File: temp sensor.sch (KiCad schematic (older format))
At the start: 28 parts, among them IC1 ESP32-C3-MINI-1, J1 Conn_01x02_Male, J2 Conn_01x04_Male, J3 Conn_01x05_Male, J4 USB_B_Micro, U2 TLV62569DBV, U3 BME280, U4 Si7020-A20, U5 SN65220

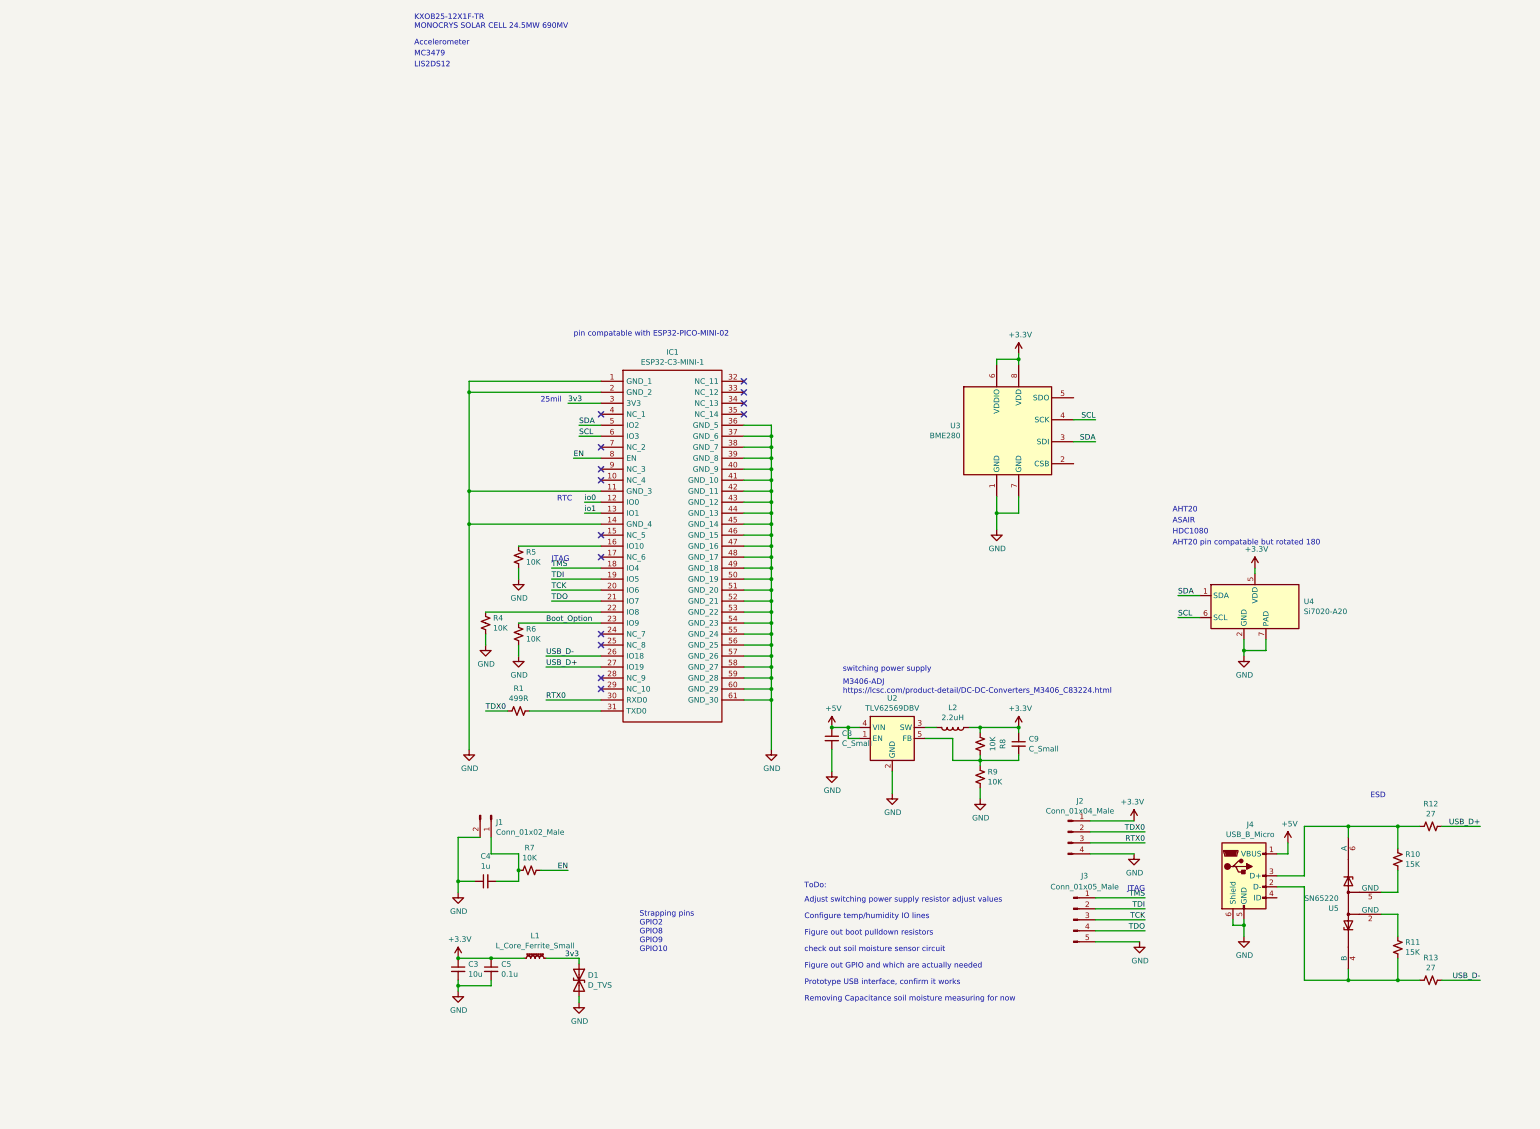
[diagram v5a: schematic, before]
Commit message: layout and part changes
Signed-off-by: lokimetasmith <lokimail@gmail.com>
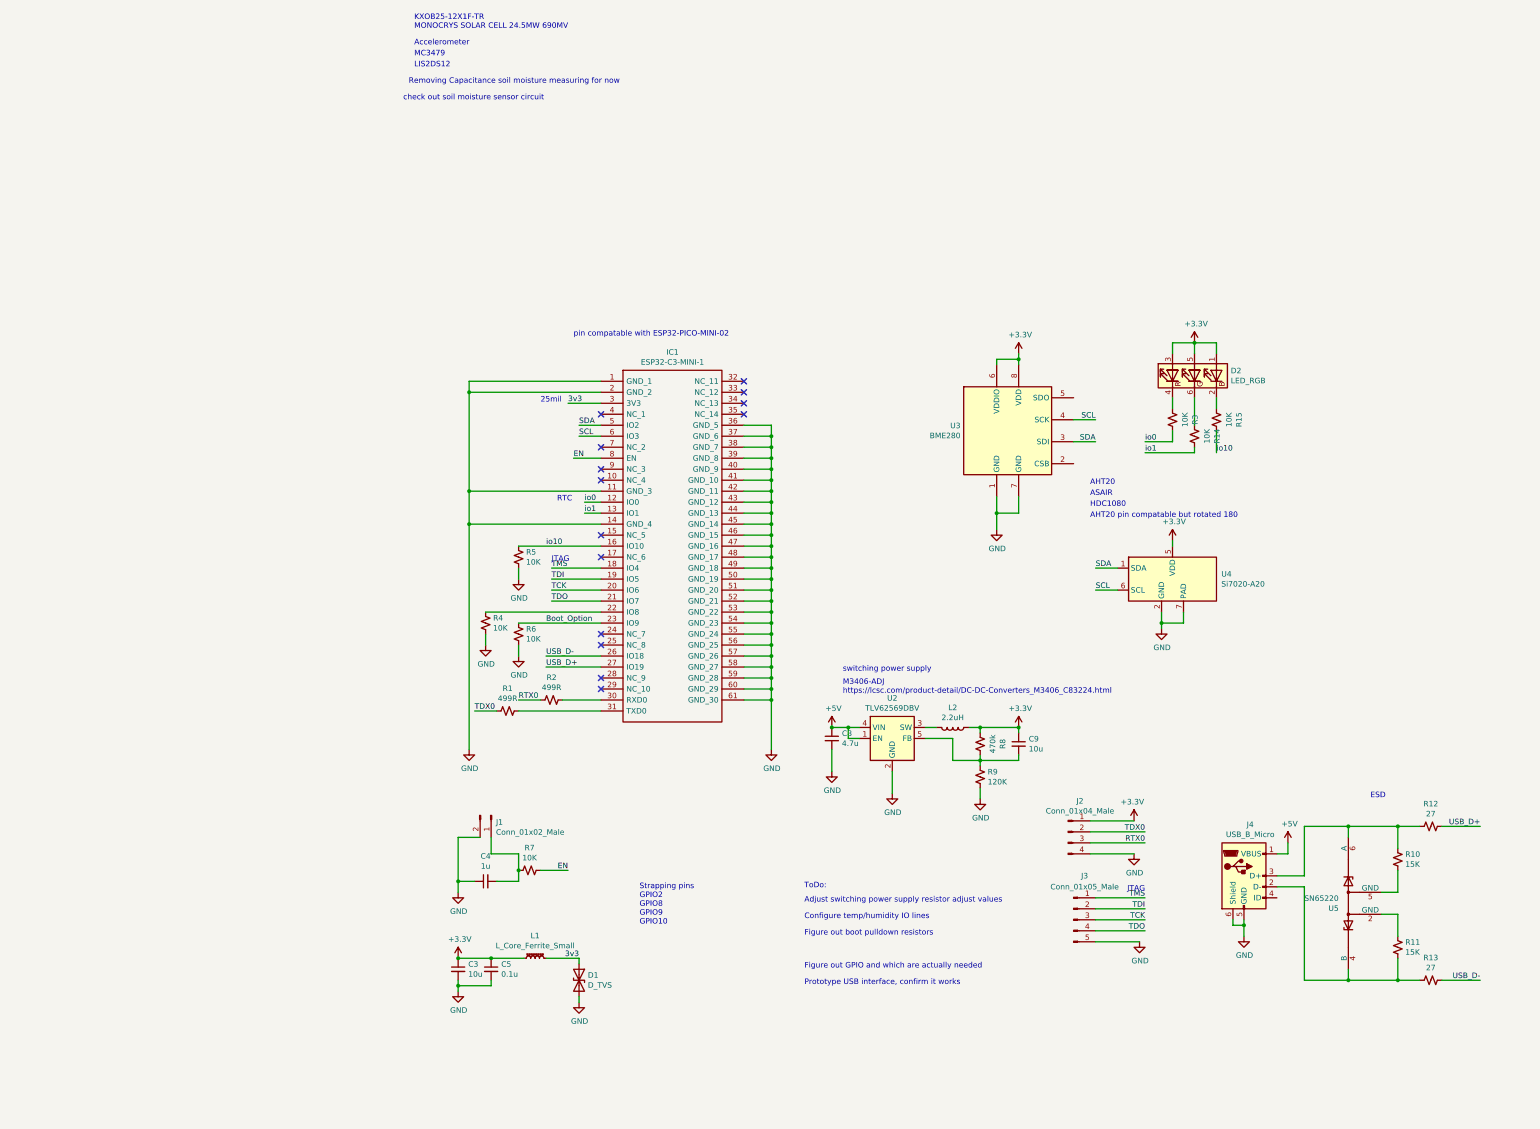
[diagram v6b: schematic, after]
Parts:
- added D2: LED_RGB, LED_SMD:LED_Cree-PLCC6_4.7x1.5mm, symbol ESP32-C3-MINI-1:LED_RGB
- added R14, R15, R3: 10K, Resistor_SMD:R_0603_1608Metric, symbol Device:R_Small_US
- added R2: 499R, Resistor_SMD:R_0603_1608Metric, symbol Device:R_Small_US
- C8: value C_Small -> 4.7u; footprint Capacitor_SMD:C_0603_1608Metric -> Capacitor_SMD:C_0805_2012Metric
- C9: value C_Small -> 10u; footprint Capacitor_SMD:C_0603_1608Metric -> Capacitor_SMD:C_0805_2012Metric
- L2: footprint Inductor_SMD:L_0603_1608Metric -> Inductor_SMD:L_Taiyo-Yuden_MD-4040
- R8: value 10K -> 470k
- R9: value 10K -> 120K
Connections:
- net +3V3: now also D2.1 (BA), D2.3 (RA), D2.5 (GA)
- net RTX0: now also R2.2; no longer IC1.30 (RXD0)
- net io0: now also R3.1
- net io1: now also R14.1
- net io10: now reaches IC1.16 (IO10), R5.1
- net io10: now also R15.1
- new net: IC1.30 (RXD0), R2.1
- new net: D2.2 (BK), R15.2
- new net: D2.4 (RK), R3.2
- new net: D2.6 (GK), R14.2
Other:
- moved on the sheet: R1, U4
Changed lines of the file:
@@
 Wire Wire Line
 	2150 3650 1650 3650
-Text Label 1650 3950 0    50   ~ 0
+Text Label 1400 3950 0    50   ~ 0
 RTX0
-Text Label 1100 4050 0    50   ~ 0
+Text Label 1000 4050 0    50   ~ 0
 TDX0
 Wire Wire Line
-	1650 3950 2150 3950
-Wire Wire Line
-	1300 4050 1100 4050
+	1400 3950 1600 3950
+Wire Wire Line
+	1200 4050 1000 4050
 $Comp
 L Connector:Conn_01x04_Male J2
@@
 F 0 "L2" V 5169 4200 50  0000 C CNN
 F 1 "2.2uH" V 5260 4200 50  0000 C CNN
-F 2 "Inductor_SMD:L_0603_1608Metric" H 5350 4200 50  0001 C CNN
+F 2 "Inductor_SMD:L_Taiyo-Yuden_MD-4040" H 5350 4200 50  0001 C CNN
 F 3 "~" H 5350 4200 50  0001 C CNN
 	1    5350 4200
@@
 Wire Wire Line
 	8000 6000 8000 5950
-Text Notes 7350 2250 0    50   ~ 0
+Text Notes 6600 2000 0    50   ~ 0
 AHT20\n
-Text Notes 7350 2350 0    50   ~ 0
+Text Notes 6600 2100 0    50   ~ 0
 ASAIR\n
 Text Label 2000 2150 0    50   ~ 0
@@
 Wire Wire Line
 	1950 6300 1650 6300
-Text Notes 2500 6250 0    50   ~ 0
+Text Notes 2500 6000 0    50   ~ 0
 Strapping pins\nGPIO2\nGPIO8\nGPIO9\nGPIO10\n
 $Comp
@@
 $EndComp
 Wire Wire Line
-	7400 3000 7600 3000
-Wire Wire Line
-	7600 3200 7400 3200
-Text Label 7400 3000 0    50   ~ 0
+	6650 2750 6850 2750
+Wire Wire Line
+	6850 2950 6650 2950
+Text Label 6650 2750 0    50   ~ 0
 SDA
-Text Label 7400 3200 0    50   ~ 0
+Text Label 6650 2950 0    50   ~ 0
 SCL
 Wire Wire Line
@@
 L power:GND #PWR024
 U 1 1 60A777B9
-P 8000 3550
-F 0 "#PWR024" H 8000 3300 50  0001 C CNN
-F 1 "GND" H 8005 3377 50  0000 C CNN
-F 2 "" H 8000 3550 50  0001 C CNN
-F 3 "" H 8000 3550 50  0001 C CNN
-	1    8000 3550
-	1    0    0    -1
-$EndComp
-Wire Wire Line
-	8000 3550 8000 3500
+P 7250 3300
+F 0 "#PWR024" H 7250 3050 50  0001 C CNN
+F 1 "GND" H 7255 3127 50  0000 C CNN
+F 2 "" H 7250 3300 50  0001 C CNN
+F 3 "" H 7250 3300 50  0001 C CNN
+	1    7250 3300
+	1    0    0    -1
+$EndComp
+Wire Wire Line
+	7250 3300 7250 3250
 $Comp
 L power:+3.3V #PWR026
 U 1 1 60AA195F
-P 8100 2750
-F 0 "#PWR026" H 8100 2600 50  0001 C CNN
-F 1 "+3.3V" H 8115 2923 50  0000 C CNN
-F 2 "" H 8100 2750 50  0001 C CNN
-F 3 "" H 8100 2750 50  0001 C CNN
-	1    8100 2750
-	1    0    0    -1
-$EndComp
-Wire Wire Line
-	8100 2750 8100 2800
+P 7350 2500
+F 0 "#PWR026" H 7350 2350 50  0001 C CNN
+F 1 "+3.3V" H 7365 2673 50  0000 C CNN
+F 2 "" H 7350 2500 50  0001 C CNN
+F 3 "" H 7350 2500 50  0001 C CNN
+	1    7350 2500
+	1    0    0    -1
+$EndComp
+Wire Wire Line
+	7350 2500 7350 2550
 $Comp
 L Regulator_Switching:TLV62569DBV U2
@@
 P 4250 4300
 F 0 "C8" H 4342 4346 50  0000 L CNN
-F 1 "C_Small" H 4342 4255 50  0000 L CNN
-F 2 "Capacitor_SMD:C_0603_1608Metric" H 4250 4300 50  0001 C CNN
+F 1 "4.7u" H 4342 4255 50  0000 L CNN
+F 2 "Capacitor_SMD:C_0805_2012Metric" H 4250 4300 50  0001 C CNN
 F 3 "~" H 4250 4300 50  0001 C CNN
 	1    4250 4300
@@
 P 5950 4350
 F 0 "C9" H 6042 4396 50  0000 L CNN
-F 1 "C_Small" H 6042 4305 50  0000 L CNN
-F 2 "Capacitor_SMD:C_0603_1608Metric" H 5950 4350 50  0001 C CNN
+F 1 "10u" H 6042 4305 50  0000 L CNN
+F 2 "Capacitor_SMD:C_0805_2012Metric" H 5950 4350 50  0001 C CNN
 F 3 "~" H 5950 4350 50  0001 C CNN
 	1    5950 4350
@@
 P 5600 4350
 F 0 "R8" V 5395 4350 50  0000 C CNN
-F 1 "10K" V 5486 4350 50  0000 C CNN
+F 1 "470k" V 5486 4350 50  0000 C CNN
 F 2 "Resistor_SMD:R_0603_1608Metric" H 5600 4350 50  0001 C CNN
 F 3 "~" H 5600 4350 50  0001 C CNN
@@
 P 5600 4650
 F 0 "R9" H 5532 4604 50  0000 R CNN
-F 1 "10K" H 5532 4695 50  0000 R CNN
+F 1 "120K" H 5532 4695 50  0000 R CNN
 F 2 "Resistor_SMD:R_0603_1608Metric" H 5600 4650 50  0001 C CNN
 F 3 "~" H 5600 4650 50  0001 C CNN
@@
 Text Notes 4000 6100 0    50   ~ 0
 Figure out boot pulldown resistors
-Text Notes 4000 6250 0    50   ~ 0
+Text Notes 350  -1500 0    50   ~ 0
 check out soil moisture sensor circuit\n
 Text Notes 4000 6400 0    50   ~ 0
@@
 L Sensor_Humidity:Si7020-A20 U4
 U 1 1 60DEE713
-P 8100 3100
-F 0 "U4" H 8544 3146 50  0000 L CNN
-F 1 "Si7020-A20" H 8544 3055 50  0000 L CNN
-F 2 "Package_DFN_QFN:DFN-6-1EP_3x3mm_P1mm_EP1.5x2.4mm" H 8100 2700 50  0001 C CNN
-F 3 "https://www.silabs.com/documents/public/data-sheets/Si7020-A20.pdf" H 7900 3400 50  0001 C CNN
-	1    8100 3100
-	1    0    0    -1
-$EndComp
-Wire Wire Line
-	8000 3500 8200 3500
-Wire Wire Line
-	8200 3500 8200 3400
-Connection ~ 8000 3500
-Wire Wire Line
-	8000 3500 8000 3400
-Text Notes 7350 2550 0    50   ~ 0
+P 7350 2850
+F 0 "U4" H 7794 2896 50  0000 L CNN
+F 1 "Si7020-A20" H 7794 2805 50  0000 L CNN
+F 2 "Package_DFN_QFN:DFN-6-1EP_3x3mm_P1mm_EP1.5x2.4mm" H 7350 2450 50  0001 C CNN
+F 3 "https://www.silabs.com/documents/public/data-sheets/Si7020-A20.pdf" H 7150 3150 50  0001 C CNN
+	1    7350 2850
+	1    0    0    -1
+$EndComp
+Wire Wire Line
+	7250 3250 7450 3250
+Wire Wire Line
+	7450 3250 7450 3150
+Connection ~ 7250 3250
+Wire Wire Line
+	7250 3250 7250 3150
+Text Notes 6600 2300 0    50   ~ 0
 AHT20 pin compatable but rotated 180
 Text Label 1950 1550 0    50   ~ 0
@@
 Wire Wire Line
 	1950 1450 2150 1450
-Text Notes 4000 6700 0    50   ~ 0
+Text Notes 400  -1650 0    50   ~ 0
 Removing Capacitance soil moisture measuring for now
 $Comp
@@
 Wire Wire Line
 	7050 6150 6650 6150
-Text Notes 7350 2450 0    50   ~ 0
+Text Notes 6600 2200 0    50   ~ 0
 HDC1080
 $Comp
@@
 L Device:R_Small_US R1
 U 1 1 609ADAE9
-P 1400 4050
-F 0 "R1" V 1195 4050 50  0000 C CNN
-F 1 "499R" V 1286 4050 50  0000 C CNN
-F 2 "Resistor_SMD:R_0603_1608Metric" H 1400 4050 50  0001 C CNN
-F 3 "~" H 1400 4050 50  0001 C CNN
-	1    1400 4050
+P 1300 4050
+F 0 "R1" V 1095 4050 50  0000 C CNN
+F 1 "499R" V 1186 4050 50  0000 C CNN
+F 2 "Resistor_SMD:R_0603_1608Metric" H 1300 4050 50  0001 C CNN
+F 3 "~" H 1300 4050 50  0001 C CNN
+	1    1300 4050
 	0    1    1    0
 $EndComp
 Wire Wire Line
-	1500 4050 2150 4050
+	1400 4050 2150 4050
 Text Notes 1600 1250 0    50   ~ 0
 25mil
+Text Label 7100 1600 0    50   ~ 0
+io0
+Text Label 7100 1700 0    50   ~ 0
+io1
+$Comp
+L ESP32-C3-MINI-1:LED_RGB D2
+U 1 1 6096940A
+P 7550 1000
+F 0 "D2" V 7596 670 50  0000 R CNN
+F 1 "LED_RGB" V 7505 670 50  0000 R CNN
+F 2 "LED_SMD:LED_Cree-PLCC6_4.7x1.5mm" H 7550 950 50  0001 C CNN
+F 3 "https://www.mouser.com/datasheet/2/723/1397_QLS6BFKW-2257848.pdf" H 7550 950 50  0001 C CNN
+	1    7550 1000
+	0    -1   -1   0
+$EndComp
+$Comp
+L Device:R_Small_US R2
+U 1 1 6096A5B0
+P 1700 3950
+F 0 "R2" V 1495 3950 50  0000 C CNN
+F 1 "499R" V 1586 3950 50  0000 C CNN
+F 2 "Resistor_SMD:R_0603_1608Metric" H 1700 3950 50  0001 C CNN
+F 3 "~" H 1700 3950 50  0001 C CNN
+	1    1700 3950
+	0    1    1    0
+$EndComp
+Wire Wire Line
+	2150 3950 1800 3950
+$Comp
+L Device:R_Small_US R3
+U 1 1 609DAEED
+P 7350 1400
+F 0 "R3" V 7145 1400 50  0000 C CNN
+F 1 "10K" V 7236 1400 50  0000 C CNN
+F 2 "Resistor_SMD:R_0603_1608Metric" H 7350 1400 50  0001 C CNN
+F 3 "~" H 7350 1400 50  0001 C CNN
+	1    7350 1400
+	-1   0    0    1
+$EndComp
+$Comp
+L Device:R_Small_US R14
+U 1 1 609DD244
+P 7550 1550
+F 0 "R14" V 7345 1550 50  0000 C CNN
+F 1 "10K" V 7436 1550 50  0000 C CNN
+F 2 "Resistor_SMD:R_0603_1608Metric" H 7550 1550 50  0001 C CNN
+F 3 "~" H 7550 1550 50  0001 C CNN
+	1    7550 1550
+	-1   0    0    1
+$EndComp
+$Comp
+L Device:R_Small_US R15
+U 1 1 609DDBCB
+P 7750 1400
+F 0 "R15" V 7545 1400 50  0000 C CNN
+F 1 "10K" V 7636 1400 50  0000 C CNN
+F 2 "Resistor_SMD:R_0603_1608Metric" H 7750 1400 50  0001 C CNN
+F 3 "~" H 7750 1400 50  0001 C CNN
+	1    7750 1400
+	-1   0    0    1
+$EndComp
+Wire Wire Line
+	7350 1600 7350 1500
+Wire Wire Line
+	7100 1600 7350 1600
+Wire Wire Line
+	7550 1700 7550 1650
+Wire Wire Line
+	7100 1700 7550 1700
+Wire Wire Line
+	7350 1300 7350 1200
+Wire Wire Line
+	7550 1200 7550 1450
+Wire Wire Line
+	7750 1300 7750 1200
+Wire Wire Line
+	7750 1500 7750 1700
+Text Label 1650 2550 0    50   ~ 0
+io10
+Text Label 7750 1700 0    50   ~ 0
+io10
+$Comp
+L power:+3.3V #PWR01
+U 1 1 60A1024F
+P 7550 700
+F 0 "#PWR01" H 7550 550 50  0001 C CNN
+F 1 "+3.3V" H 7565 873 50  0000 C CNN
+F 2 "" H 7550 700 50  0001 C CNN
+F 3 "" H 7550 700 50  0001 C CNN
+	1    7550 700
+	1    0    0    -1
+$EndComp
+Wire Wire Line
+	7350 800  7350 700
+Wire Wire Line
+	7350 700  7550 700
+Wire Wire Line
+	7550 700  7550 800
+Connection ~ 7550 700
+Wire Wire Line
+	7550 700  7750 700
+Wire Wire Line
+	7750 700  7750 800
 $EndSCHEMATC

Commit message: Signed-off-by: lokimetasmith <lokimail@gmail.com>
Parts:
- D2: symbol ESP32-C3-MINI-1:LED_RGB -> Device:LED_RGB
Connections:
- net +3V3: now also D2.4 (BA), D2.6 (RA); no longer D2.1 (BA), D2.3 (RA)
- net at D2.2 (GK): now also R14.2; no longer R15.2
- net at R3.2: now also D2.1 (RK); no longer D2.4 (RK)
- new net: D2.3 (BK), R15.2
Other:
- moved on the sheet: U4
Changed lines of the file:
@@
 Wire Wire Line
 	8000 6000 8000 5950
-Text Notes 6600 2000 0    50   ~ 0
+Text Notes 8850 1850 0    50   ~ 0
 AHT20\n
-Text Notes 6600 2100 0    50   ~ 0
+Text Notes 8850 1950 0    50   ~ 0
 ASAIR\n
 Text Label 2000 2150 0    50   ~ 0
@@
 $EndComp
 Wire Wire Line
-	6650 2750 6850 2750
-Wire Wire Line
-	6850 2950 6650 2950
-Text Label 6650 2750 0    50   ~ 0
+	8550 2750 8750 2750
+Wire Wire Line
+	8750 2950 8550 2950
+Text Label 8550 2750 0    50   ~ 0
 SDA
-Text Label 6650 2950 0    50   ~ 0
+Text Label 8550 2950 0    50   ~ 0
 SCL
 Wire Wire Line
@@
 L power:GND #PWR024
 U 1 1 60A777B9
-P 7250 3300
-F 0 "#PWR024" H 7250 3050 50  0001 C CNN
-F 1 "GND" H 7255 3127 50  0000 C CNN
-F 2 "" H 7250 3300 50  0001 C CNN
-F 3 "" H 7250 3300 50  0001 C CNN
-	1    7250 3300
-	1    0    0    -1
-$EndComp
-Wire Wire Line
-	7250 3300 7250 3250
+P 9150 3300
+F 0 "#PWR024" H 9150 3050 50  0001 C CNN
+F 1 "GND" H 9155 3127 50  0000 C CNN
+F 2 "" H 9150 3300 50  0001 C CNN
+F 3 "" H 9150 3300 50  0001 C CNN
+	1    9150 3300
+	1    0    0    -1
+$EndComp
+Wire Wire Line
+	9150 3300 9150 3250
 $Comp
 L power:+3.3V #PWR026
 U 1 1 60AA195F
-P 7350 2500
-F 0 "#PWR026" H 7350 2350 50  0001 C CNN
-F 1 "+3.3V" H 7365 2673 50  0000 C CNN
-F 2 "" H 7350 2500 50  0001 C CNN
-F 3 "" H 7350 2500 50  0001 C CNN
-	1    7350 2500
-	1    0    0    -1
-$EndComp
-Wire Wire Line
-	7350 2500 7350 2550
+P 9250 2500
+F 0 "#PWR026" H 9250 2350 50  0001 C CNN
+F 1 "+3.3V" H 9265 2673 50  0000 C CNN
+F 2 "" H 9250 2500 50  0001 C CNN
+F 3 "" H 9250 2500 50  0001 C CNN
+	1    9250 2500
+	1    0    0    -1
+$EndComp
+Wire Wire Line
+	9250 2500 9250 2550
 $Comp
 L Regulator_Switching:TLV62569DBV U2
@@
 L Sensor_Humidity:Si7020-A20 U4
 U 1 1 60DEE713
-P 7350 2850
-F 0 "U4" H 7794 2896 50  0000 L CNN
-F 1 "Si7020-A20" H 7794 2805 50  0000 L CNN
-F 2 "Package_DFN_QFN:DFN-6-1EP_3x3mm_P1mm_EP1.5x2.4mm" H 7350 2450 50  0001 C CNN
-F 3 "https://www.silabs.com/documents/public/data-sheets/Si7020-A20.pdf" H 7150 3150 50  0001 C CNN
-	1    7350 2850
-	1    0    0    -1
-$EndComp
-Wire Wire Line
-	7250 3250 7450 3250
-Wire Wire Line
-	7450 3250 7450 3150
-Connection ~ 7250 3250
-Wire Wire Line
-	7250 3250 7250 3150
-Text Notes 6600 2300 0    50   ~ 0
+P 9250 2850
+F 0 "U4" H 9694 2896 50  0000 L CNN
+F 1 "Si7020-A20" H 9694 2805 50  0000 L CNN
+F 2 "Package_DFN_QFN:DFN-6-1EP_3x3mm_P1mm_EP1.5x2.4mm" H 9250 2450 50  0001 C CNN
+F 3 "https://www.silabs.com/documents/public/data-sheets/Si7020-A20.pdf" H 9050 3150 50  0001 C CNN
+	1    9250 2850
+	1    0    0    -1
+$EndComp
+Wire Wire Line
+	9150 3250 9350 3250
+Wire Wire Line
+	9350 3250 9350 3150
+Connection ~ 9150 3250
+Wire Wire Line
+	9150 3250 9150 3150
+Text Notes 8850 2150 0    50   ~ 0
 AHT20 pin compatable but rotated 180
 Text Label 1950 1550 0    50   ~ 0
@@
 Wire Wire Line
 	7050 6150 6650 6150
-Text Notes 6600 2200 0    50   ~ 0
+Text Notes 8850 2050 0    50   ~ 0
 HDC1080
 $Comp
@@
 io1
 $Comp
-L ESP32-C3-MINI-1:LED_RGB D2
+L Device:LED_RGB D2
 U 1 1 6096940A
 P 7550 1000
